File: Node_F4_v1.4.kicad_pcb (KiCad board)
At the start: 2 copper layers, 95 x 58.5 mm, 87 parts, among them J1 Screw_Terminal_01x02, J3 Screw_Terminal_01x02, J4 Screw_Terminal_01x02, J5 Screw_Terminal_01x03, J6 Conn_01x16_Female, J7 Conn_01x08_Male, J8 STLINK, Q1 P_Mosfet, U10 Ai-Thinker-Ra-02, U2 PCF8574A, U3 AMS1117-3.3, U4 DS3231M, U5 MAX485E, U6 STM32F411CEUx, U7 Trans_MOSFET, U8 Trans_MOSFET, U9 W25Q128JVS, Y1 25MHz

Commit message: sua nguon
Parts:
- removed RST: SW_Push, IVS_FOOTPRINTS:SW_SPST_PTS810
- added SW1: SW_Push, IVS_FOOTPRINTS:SW_SPST_PTS810, F.Cu at (122.6, 53.0)
- J6, J7: moved to B.Cu
- R19: footprint Resistor_SMD:R_0603_1608Metric -> Resistor_SMD:R_0805_2012Metric
- moved L1 20.3 mm to (101.8, 83.5), turned to -90 degrees
- moved C1 17.7 mm to (88.4, 80.0), turned to -90 degrees
- moved RV1 15.3 mm to (79.7, 87.4), turned to 90 degrees
- moved F1 1.24 mm to (79.4, 98.7)
- moved RL2 0.74 mm to (111.5, 95.5)
- moved RL1 0.47 mm to (120.0, 95.5)
- moved J7 0.13 mm to (147.1, 52.0), turned to -90 degrees
- moved R19 0.11 mm to (167.1, 79.4)
- moved Q1 0.08 mm to (162.9, 78.4)
- turned J6 to 180 degrees
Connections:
- J3 pad 1: /N -> /N2
- J3 pad 2: /relay_2 -> /L
- J4 pad 1: /N -> /N1
- J4 pad 2: /relay_1 -> /L
- RL1 pad 2: /relay_1 -> /N
- RL1 pad 3: /N -> /N1
- RL2 pad 2: /relay_2 -> /N
- RL2 pad 3: /N -> /N2
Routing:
- net /L: track 10.9 -> 49.5 mm
- net Net-(L1-Pad3): track 18.5 -> 40.0 mm
- net /relay_2: track 17.2 -> 0.00 mm
- net /relay_1: track 15.8 -> 0.00 mm
- net Net-(L1-Pad1): track 21.4 -> 37.1 mm
- net /N: track 79.2 -> 65.0 mm
- net Net-(C1-Pad1): track 25.8 -> 39.3 mm
- net /N2: track 0.00 -> 12.2 mm
- net /N1: track 0.00 -> 9.37 mm
- net Net-(D10-Pad1): track 12.1 -> 11.3 mm
- net Net-(Q1-Pad2): track 7.43 -> 7.99 mm
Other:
- outline, holes or cut-outs redrawn
- board text added: "B- GND A+"
- board text removed: "RS485"

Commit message: thay terminal
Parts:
- removed J3, J4: Screw_Terminal_01x02, TerminalBlock_Phoenix:TerminalBlock_Phoenix_MKDS-1,5-2-5.08_1x02_P5.08mm_Horizontal
- removed J5: Screw_Terminal_01x03, TerminalBlock_Phoenix:TerminalBlock_Phoenix_MKDS-1,5-3-5.08_1x03_P5.08mm_Horizontal
- J1: value Screw_Terminal_01x02 -> Screw_Terminal_01x09; footprint TerminalBlock_Phoenix:TerminalBlock_Phoenix_MKDS-1,5-2-5.08_1x02_P5.08mm_Horizontal -> TerminalBlock_Phoenix:TerminalBlock_Phoenix_MKDS-1,5-9_1x09_P5.00mm_Horizontal
- moved J1 6.85 mm to (93.5, 102.8)
- moved J6 0.18 mm to (170.0, 59.4)
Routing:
- net /N2: track 12.2 -> 8.41 mm
- net /N: track 65.0 -> 62.0 mm
- net /N1: track 9.37 -> 7.82 mm
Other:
- outline, holes or cut-outs redrawn
- board text added: "~220V"
- board text removed: "N-L"

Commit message: teardrop
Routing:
- net +3.3V: track 251.1 -> 241.8 mm
- net Net-(C13-Pad2): track 51.3 -> 48.7 mm
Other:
- outline, holes or cut-outs redrawn

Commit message: chinh via
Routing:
- net +5V: track 222.5 -> 217.0 mm, vias 19 -> 21
- net +3.3V: track 241.8 -> 242.7 mm, vias 21 -> 23
- net GND: vias 314 -> 363
- added copper zone on F.Cu, net +5V
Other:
- outline, holes or cut-outs redrawn

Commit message: DONE
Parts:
- removed R18: 1K, Resistor_SMD:R_0603_1608Metric
- added BZ1: Buzzer, Buzzer_Beeper:PUIAudio_SMT_0825_S_4_R, F.Cu at (140.3, 78.8)
- added Q2: MMBT3904L, IVS_FOOTPRINTS:SOT23-3, F.Cu at (144.5, 71.8)
- R19: value 100R -> 1K; footprint Resistor_SMD:R_0805_2012Metric -> Resistor_SMD:R_0603_1608Metric
- moved R19 23.9 mm to (145.2, 69.8), turned to 135 degrees
- moved C11 9.41 mm to (152.9, 71.7), turned to -135 degrees
- moved C12 9.38 mm to (150.7, 73.9), turned to 45 degrees
- moved C21 5.88 mm to (147.8, 78.2)
- moved C13 5.88 mm to (146.7, 75.0), turned to 135 degrees
- moved C15 5.88 mm to (154.4, 74.5)
- moved C16 5.88 mm to (153.6, 86.5)
- moved C17 5.88 mm to (155.5, 87.8)
- moved C18 5.88 mm to (160.7, 82.1)
- moved C19 5.88 mm to (156.6, 74.5)
- moved C20 5.88 mm to (148.9, 77.1)
- moved R20 5.88 mm to (152.0, 74.7)
- moved R7 5.88 mm to (145.7, 76.0), turned to 135 degrees
- moved U6 5.88 mm to (154.9, 80.9)
- moved R17 5.75 mm to (166.8, 80.2), turned to 180 degrees
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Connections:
- J6 pad 8: Net-(J6-Pad8) -> +3.3V
- Q1 pad 2: Net-(Q1-Pad2) -> GND
- Q1 pad 3: +5V -> +3.3V
- R17 pad 1: Net-(Q1-Pad2) -> GND
- R19 pad 1: Net-(Q1-Pad2) -> Net-(Q2-Pad1)
- R19 pad 2: Net-(J6-Pad8) -> /BUZZER
- U6 pad 2: unconnected-(U6-Pad2) -> /BUZZER
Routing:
- net +5V: track 217.0 -> 33.5 mm, vias 21 -> 33
- net /SWCLK: track 39.4 -> 55.5 mm, vias 2 -> 1
- net /BUZZER: track 0.00 -> 15.1 mm, vias 0 -> 2
- net /SWDIO: track 42.8 -> 57.7 mm, vias 2 -> 1
- net /RS485_DERE: track 19.8 -> 32.6 mm
- net /RX_RS485: track 15.9 -> 28.5 mm
- net /TX_RS485: track 20.4 -> 30.0 mm, vias 2 -> 0
- net /SDA: track 40.4 -> 48.7 mm
- net /SCL: track 44.5 -> 52.7 mm
- net Net-(C13-Pad2): track 48.7 -> 56.8 mm
- net /RELAY_2: track 34.3 -> 42.0 mm
- net Net-(Q1-Pad2): track 7.52 -> 0.00 mm
- net /RELAY_1: track 42.9 -> 49.7 mm
- net Net-(C2-Pad2): track 6.78 -> 0.00 mm
- net /TFT_DB2: track 20.9 -> 14.7 mm
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- added copper zone on B.Cu, net +5V
- added copper zone on F.Cu, net Net-(C2-Pad2)
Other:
- outline, holes or cut-outs redrawn
- board text added: "5v 3v3 GND DIO SCK"
- board text added: "B- EARTH A+"
- board text removed: "5v 3v3 GND DIO CLK"
- board text removed: "B- GND A+"

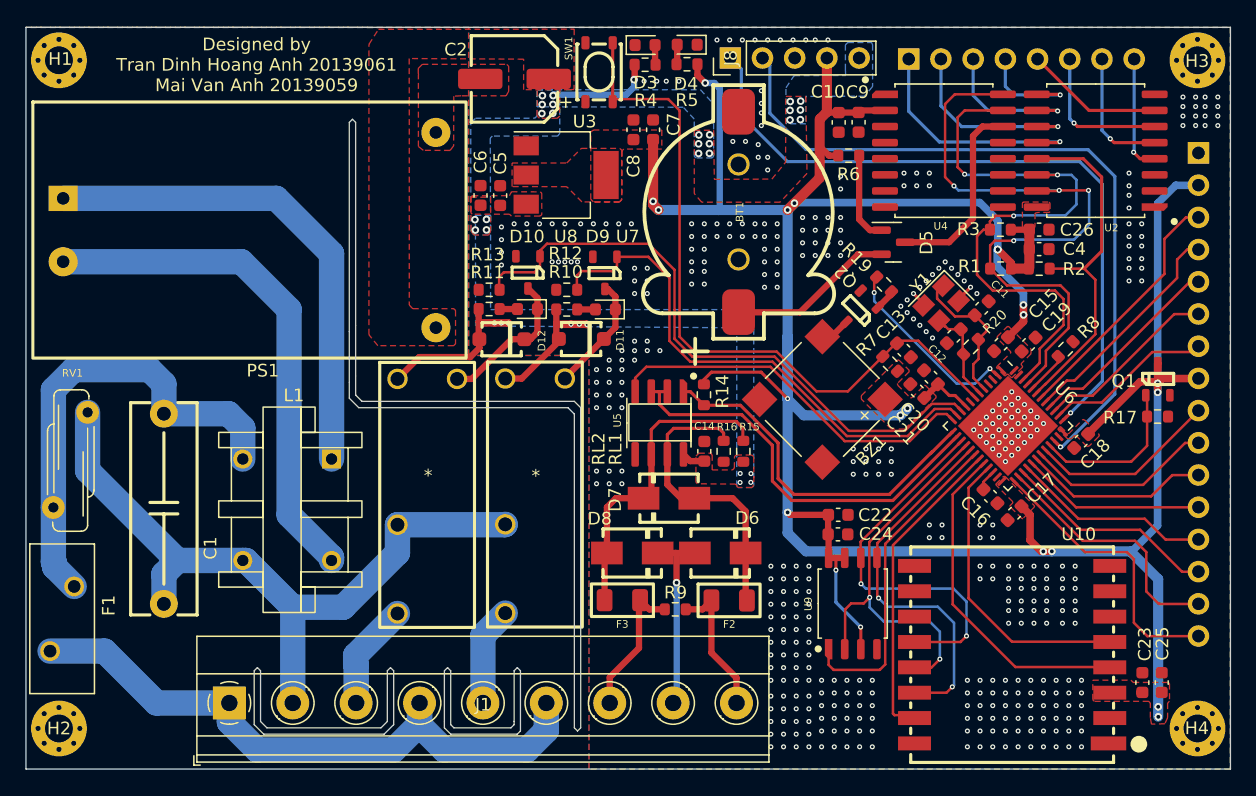
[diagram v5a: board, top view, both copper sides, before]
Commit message: Fix GND alu cap at output HLK
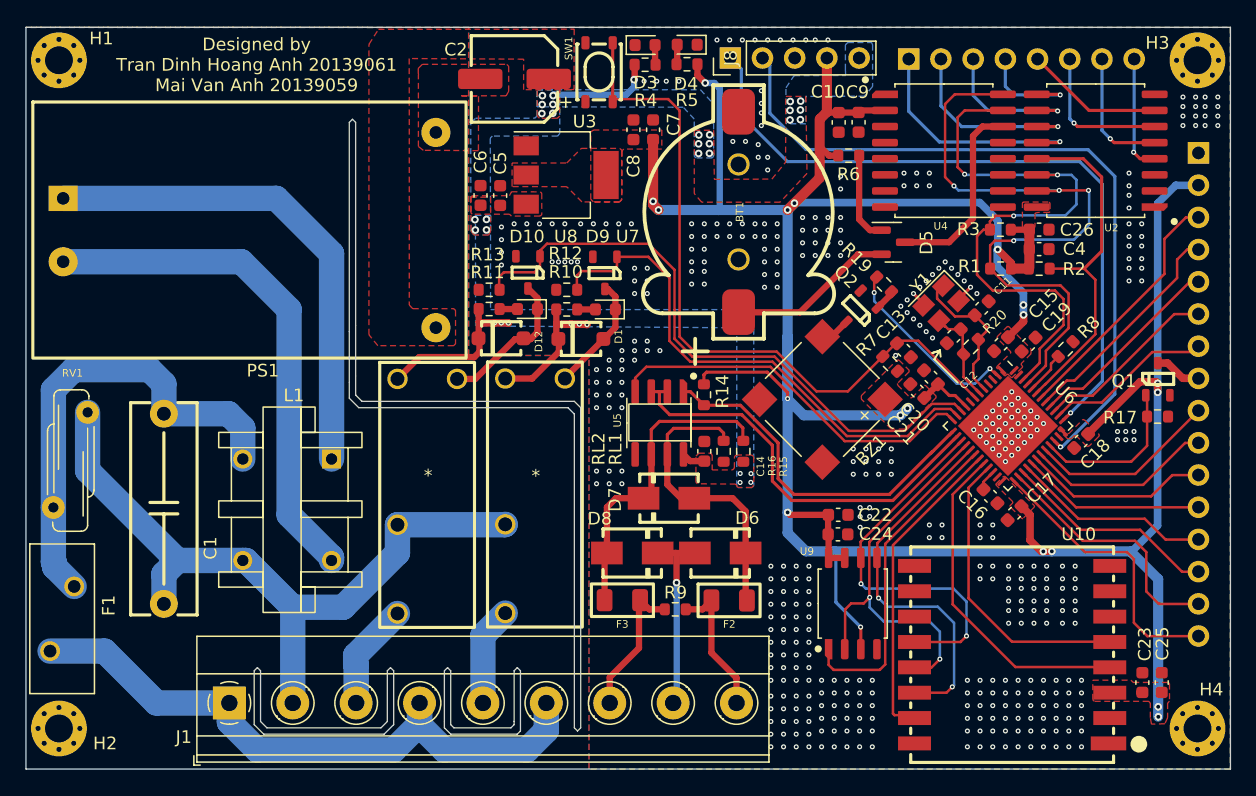
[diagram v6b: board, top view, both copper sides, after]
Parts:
- removed D11: D_Diode, IVS_FOOTPRINTS:D_SOD-123F
- added D1: D_Schottky, IVS_FOOTPRINTS:D_SOD-123F, F.Cu at (121.3, 74.1)
- D12: value D_Diode -> D_Schottky
- moved D12 0.07 mm to (115.0, 74.0), turned to 0 degrees
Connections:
- C2 pad 2: Net-(C2-Pad2) -> GND
- D12 pad 1: Net-(D10-Pad1) -> +5V
- D12 pad 2: +5V -> Net-(D10-Pad1)
- J6 pad 8: +3.3V -> Net-(J6-Pad8)
- PS1 pad 3: Net-(C2-Pad2) -> GND
- Q1 pad 3: +3.3V -> Net-(J6-Pad8)
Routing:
- net +3.3V: track 247.0 -> 243.2 mm, vias 21 -> 19
- net Net-(J6-Pad8): track 0.00 -> 3.72 mm
- net +5V: track 33.5 -> 34.2 mm
- net GND: vias 434 -> 446
- removed copper zone on F.Cu, net Net-(C2-Pad2)
